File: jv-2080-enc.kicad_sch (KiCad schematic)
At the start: 9 parts

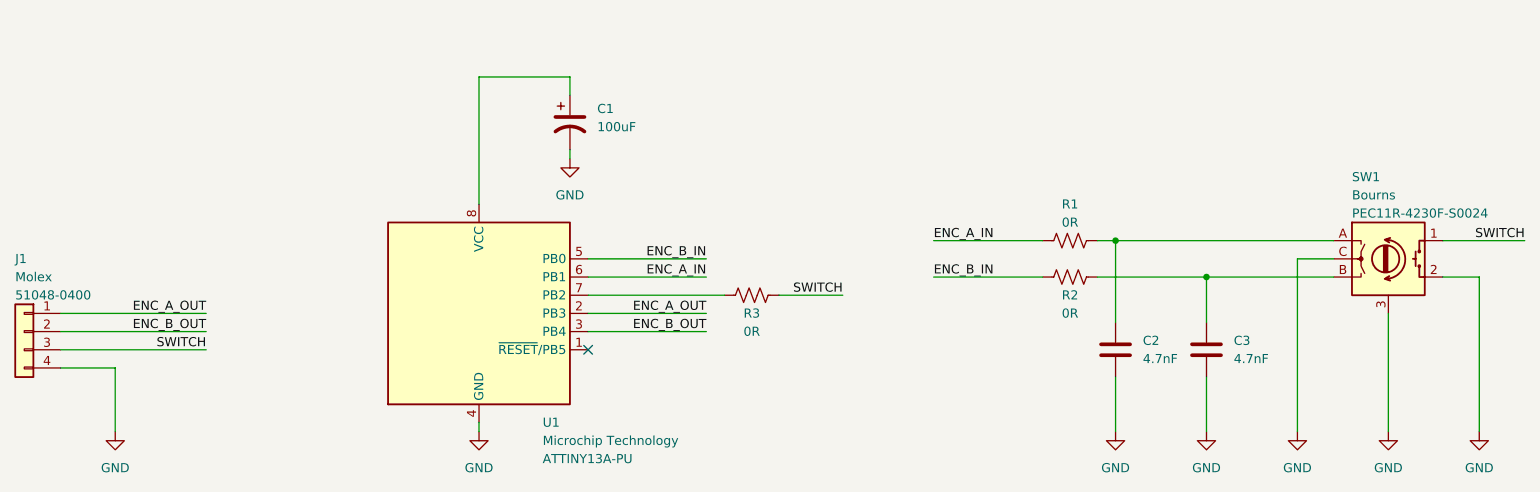
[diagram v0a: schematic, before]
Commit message: Re-drew the schematic to be easier to read. Tweaked the layout so that the PCB is 2mm less wide.
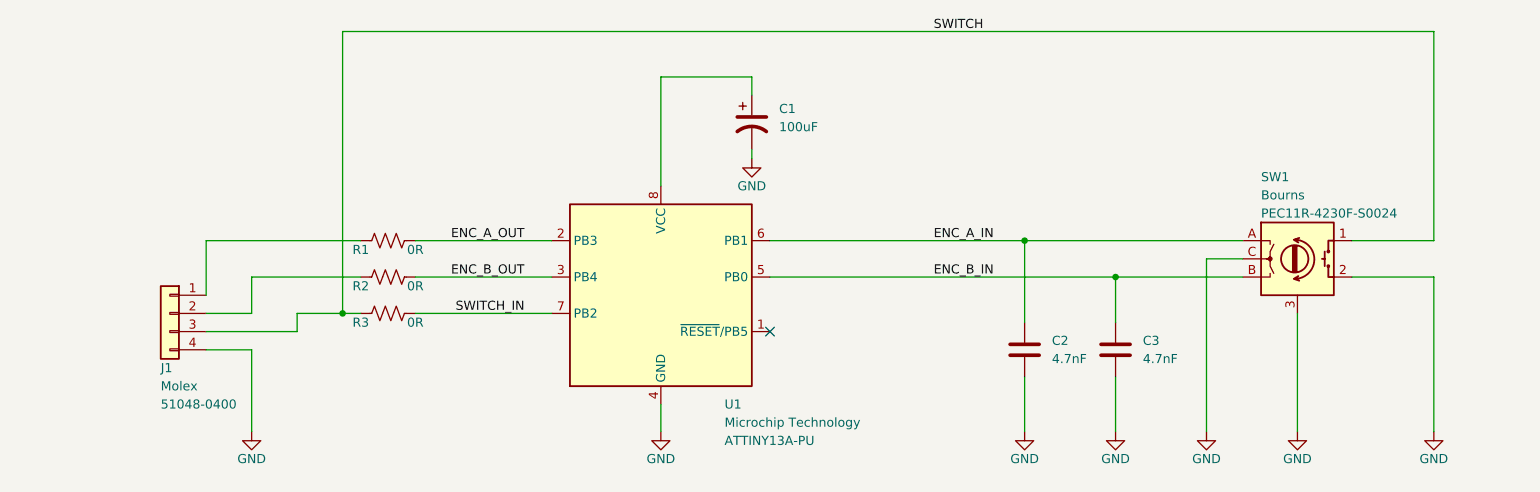
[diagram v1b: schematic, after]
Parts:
- J1: value (none) -> Conn_01x04; footprint (none) -> encoders:Molex_51048-0400
- SW1: value (none) -> RotaryEncoder_Switch; footprint (none) -> encoders:Rotary_Encoder_Switched_PEC11R
- U1: value (none) -> ATtiny13A-P; footprint (none) -> Package_DIP:DIP-8_W7.62mm
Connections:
- net ENC_A_IN: now also C2.1, SW1.A; no longer R1.1
- net ENC_A_OUT: now also R1.2; no longer J1.1 (Pin_1)
- net ENC_B_IN: now also C3.1, SW1.B; no longer R2.1
- net ENC_B_OUT: now also R2.2; no longer J1.2 (Pin_2)
- net SWITCH: now also R3.1; no longer R3.2
- net SWITCH_IN: now reaches U1.7 (PB2)
- net SWITCH_IN: now also R3.2; no longer R3.1
- new net: J1.1 (Pin_1), R1.1
- new net: J1.2 (Pin_2), R2.1
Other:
- moved on the sheet: C1, C2, C3, J1, SW1, U1
